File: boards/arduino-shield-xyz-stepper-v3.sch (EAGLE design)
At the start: 10 parts, among them IC1 2967-MP6500, IC2 2967-MP6500, IC3 2967-MP6500, J4 ARDUINO_R3_SHIELD, J6 455-1750-1-ND

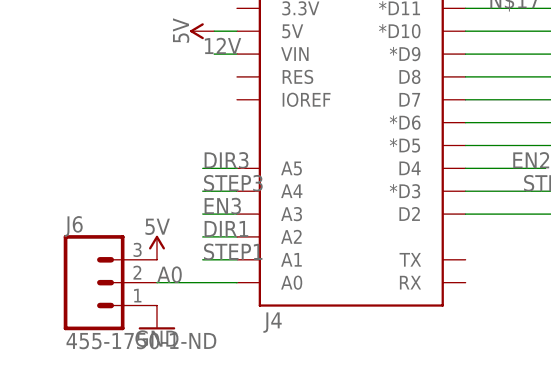
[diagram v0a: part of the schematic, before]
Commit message: better robot code, new board version
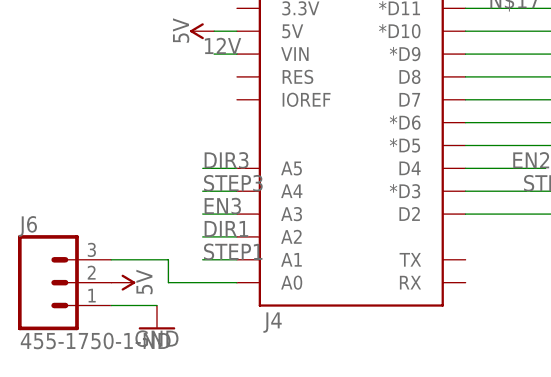
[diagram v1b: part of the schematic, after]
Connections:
- removed net A0: J4.A0, J6.2
- new net N$15: J4.A0, J6.3
- net 5V: now also J6.2; no longer J6.3
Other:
- moved on the sheet: J6
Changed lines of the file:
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@@
 <setting verticaltext="up"/>
 </settings>
-<grid distance="0.05" unitdist="inch" unit="inch" style="lines" multiple="1" display="yes" altdistance="0.01" altunitdist="inch" altunit="inch"/>
+<grid distance="0.025" unitdist="inch" unit="inch" style="lines" multiple="1" display="yes" altdistance="0.01" altunitdist="inch" altunit="inch"/>
 <layers>
 <layer number="1" name="Top" color="4" fill="1" visible="no" active="no"/>
@@
 <attribute name="VALUE" x="107.95" y="121.666" size="1.778" layer="96" align="top-center"/>
 </instance>
-<instance part="J6" gate="J$1" x="31.75" y="72.39"/>
+<instance part="J6" gate="J$1" x="26.67" y="72.39"/>
 <instance part="GND5" gate="1" x="39.37" y="67.31" smashed="yes">
 <attribute name="VALUE" x="39.37" y="67.056" size="1.778" layer="96" align="top-center"/>
 </instance>
-<instance part="SUPPLY8" gate="G$1" x="39.37" y="74.93"/>
+<instance part="SUPPLY8" gate="G$1" x="34.29" y="72.39" rot="R270"/>
 </instances>
 <busses>
@@
 <pinref part="J6" gate="J$1" pin="1"/>
 <pinref part="GND5" gate="1" pin="GND"/>
+<wire x1="34.29" y1="69.85" x2="39.37" y2="69.85" width="0.1524" layer="91"/>
 </segment>
 </net>
@@
 </segment>
 <segment>
-<pinref part="J6" gate="J$1" pin="3"/>
+<pinref part="J6" gate="J$1" pin="2"/>
 <pinref part="SUPPLY8" gate="G$1" pin="5V"/>
 </segment>
@@
 </segment>
 </net>
-<net name="A0" class="0">
+<net name="N$15" class="0">
 <segment>
 <pinref part="J4" gate="G$1" pin="A0"/>
-<wire x1="48.26" y1="72.39" x2="39.37" y2="72.39" width="0.1524" layer="91"/>
-<label x="39.37" y="72.39" size="1.778" layer="95"/>
-<pinref part="J6" gate="J$1" pin="2"/>
-</segment>
-</net>
+<wire x1="48.26" y1="72.39" x2="40.64" y2="72.39" width="0.1524" layer="91"/>
+<pinref part="J6" gate="J$1" pin="3"/>
+<wire x1="34.29" y1="74.93" x2="40.64" y2="74.93" width="0.1524" layer="91"/>
+<wire x1="40.64" y1="74.93" x2="40.64" y2="72.39" width="0.1524" layer="91"/>
+</segment>
+</net>
